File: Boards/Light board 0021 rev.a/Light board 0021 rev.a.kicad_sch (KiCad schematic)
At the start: 43 parts, among them J1 card edge, J2 light connector, Q1 2N6125, U1 2.2K, U1 6821, U2 2.2K, U4 ULN2003A, U5 7406, U6 Board ID header

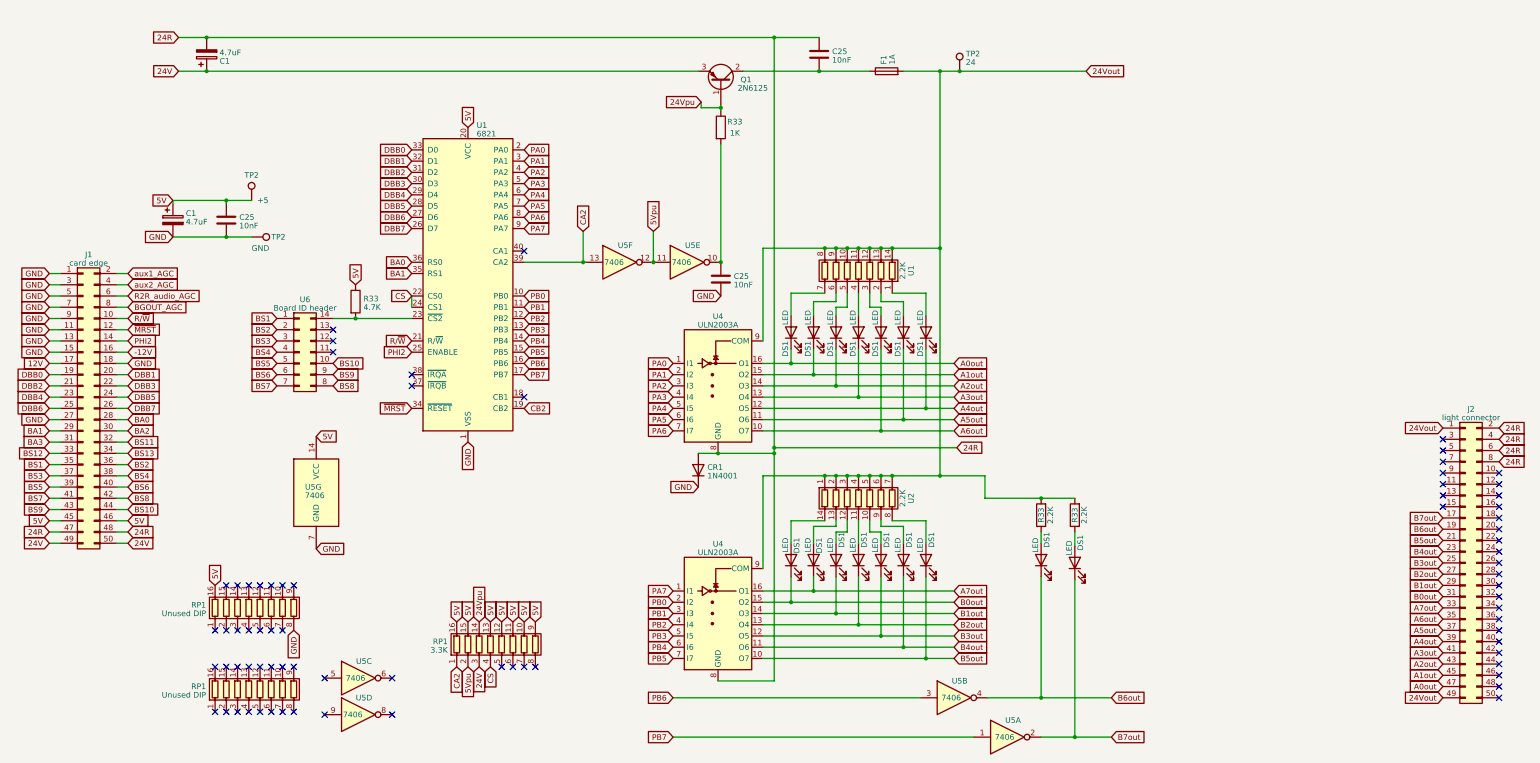
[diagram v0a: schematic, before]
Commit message: finish light board rev.a, rename files, add renders and schematics, move pictures
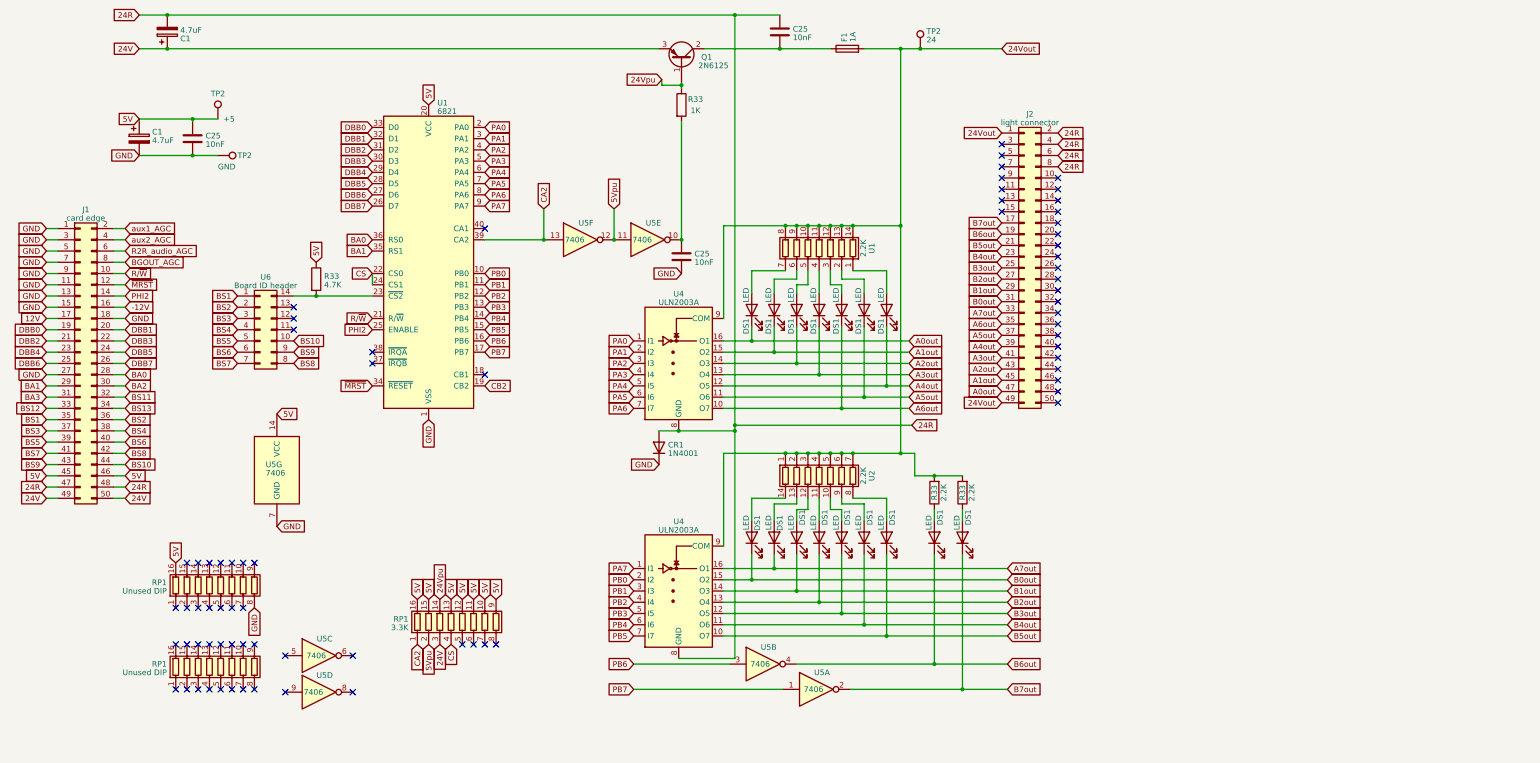
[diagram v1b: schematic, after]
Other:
- moved on the sheet: C1, C25, CR1, DS1, F1, J1, J2, Q1, R33, RP1, TP2, U1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
